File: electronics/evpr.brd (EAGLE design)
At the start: 97.2 x 41.3 mm, 115 parts, among them J1 10118193-0001LF, J2 B4P-VH(LF)(SN), Q1 AOD4184A, Q2 AOD4184A, T3 MMBT2222A, T5 MMBT2222A, U1 BQ2057TTS, U3 ESP32-WROOM-32D, U6 SN74AHCT125DR, U7 TPSM84824MOLR, U8 LTC4353CMSPBFMSOP-16_MS-M, X1 B3P-VH(LF)(SN), X2 B3P-VH(LF)(SN), X3 B3P-VH(LF)(SN)

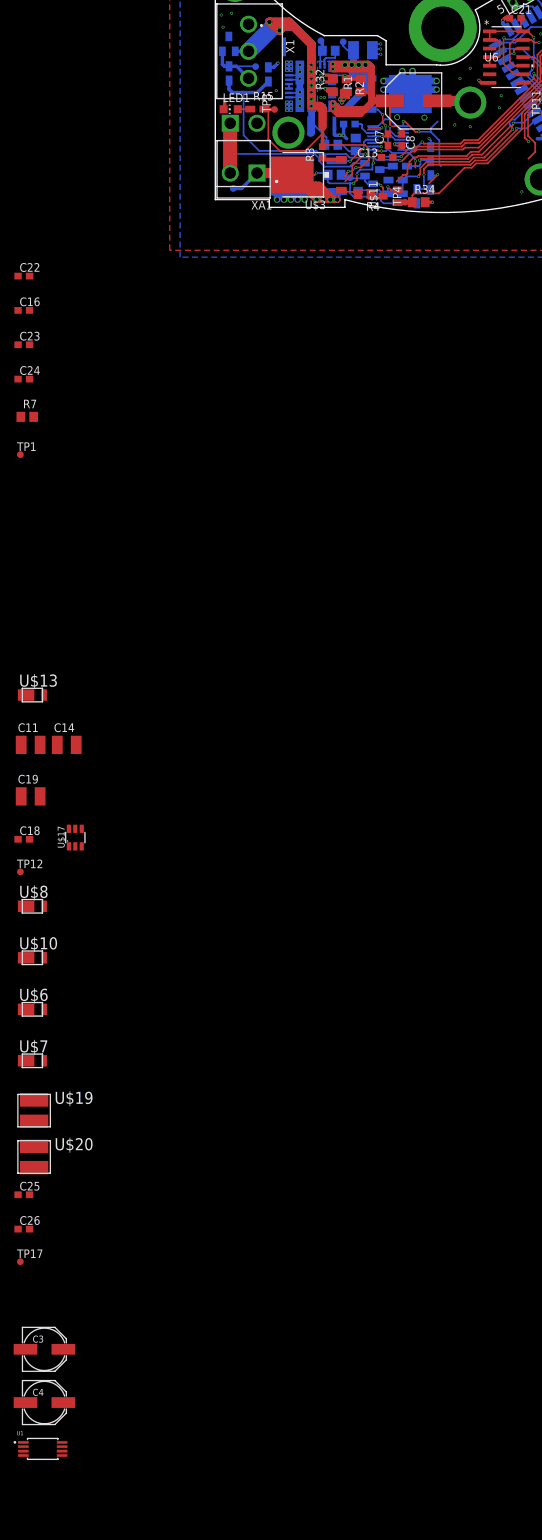
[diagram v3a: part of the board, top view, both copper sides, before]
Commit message: Replaced R31 and R2 with R8 and R32 respectively, 0603 outline and corrected part selection.
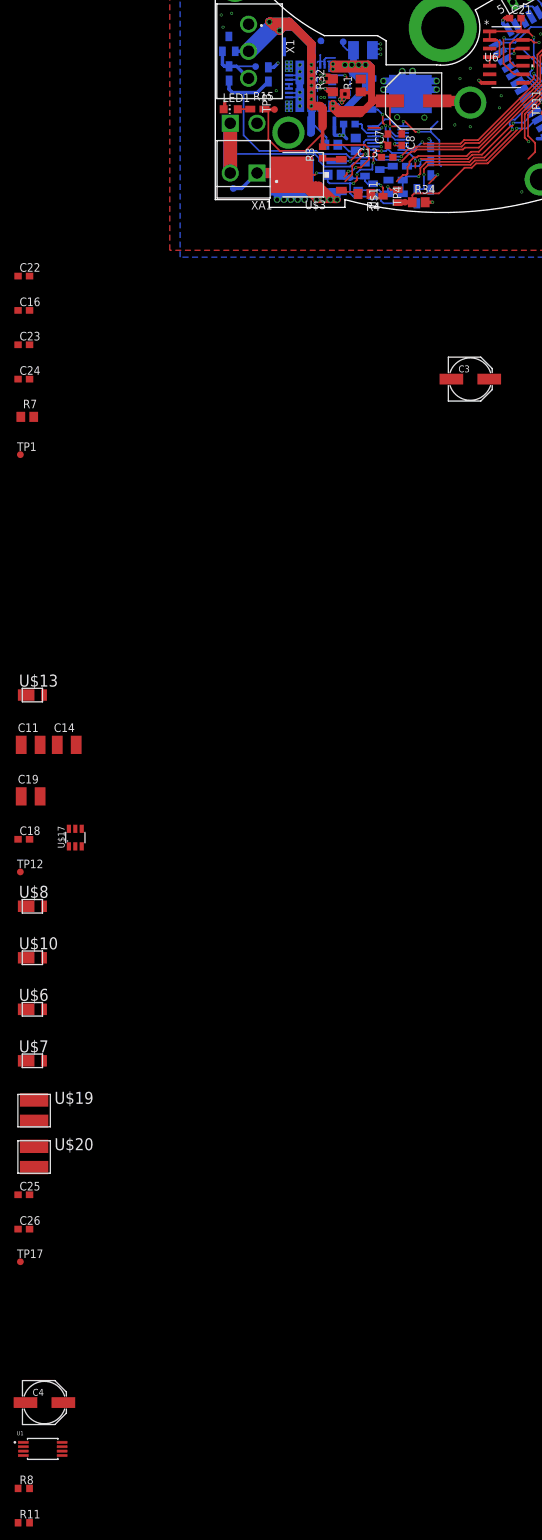
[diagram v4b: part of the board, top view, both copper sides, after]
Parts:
- removed R2: 768Ω 1%, rcl:R0805
- removed R31: 37.4kΩ 1%, rcl:R0805
- added R11: 768Ω 1%, rcl:R0603
- added R8: 37.4kΩ 1%, rcl:R0603
- moved C3 156.7 mm to (4.06, -80.5)
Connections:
- net AGND: now also R11.1, R8.1; no longer R2.2, R31.2
- net N$17: now also R8.2; no longer R31.1
- net N$3: now also R11.2; no longer R2.1
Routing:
- net N$3: track 4.60 -> 2.28 mm
- net AGND: track 12.9 -> 11.0 mm
- net N$17: track 3.54 -> 2.47 mm
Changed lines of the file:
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@@
 <attribute name="VALUE" x="-9.6012" y="-37.719" size="1.27" layer="27" rot="R90"/>
-</element>
-<element name="R2" library="rcl" package="R0805" value="768Ω 1%" x="-14.1986" y="-37.084" smashed="yes" rot="R270">
-<attribute name="COMPONENT" value="RC0402FR-07768RL" x="-14.1986" y="-37.084" size="1.778" layer="27" rot="R270" display="off"/>
-<attribute name="NAME" x="-12.9286" y="-36.449" size="1.27" layer="25" rot="R270"/>
-<attribute name="VALUE" x="-16.7386" y="-36.449" size="1.27" layer="27" rot="R270"/>
-</element>
-<element name="R31" library="rcl" package="R0805" value="37.4kΩ 1%" x="-16.8656" y="-31.9532" smashed="yes" rot="MR0">
-<attribute name="COMPONENT" value="RC0201FR-0737K4L" x="-16.8656" y="-31.9532" size="1.778" layer="28" rot="MR0" display="off"/>
-<attribute name="NAME" x="-16.2306" y="-30.6832" size="1.27" layer="26" rot="MR0"/>
-<attribute name="VALUE" x="-16.2306" y="-34.4932" size="1.27" layer="28" rot="MR0"/>
 </element>
 <element name="C1" library="mccloud" package="CAP_3225" value="10µF" x="-21.59" y="-31.369" smashed="yes" rot="MR180">
@@
 <attribute name="VALUE" x="-62.865" y="-211.582" size="0.0254" layer="27"/>
 </element>
-<element name="C3" library="mccloud" package="OSCON_SVPF_6.3MM" value="56µF" x="-58.928" y="-224.028" smashed="yes">
-<attribute name="COMPONENT" value="APXG250ARA560MF61G" x="-58.928" y="-224.028" size="1.778" layer="27" display="off"/>
-<attribute name="NAME" x="-60.680890625" y="-223.02635" size="1.01768125" layer="25"/>
-<attribute name="VALUE" x="-60.67856875" y="-226.003640625" size="1.01633125" layer="27"/>
+<element name="C3" library="mccloud" package="OSCON_SVPF_6.3MM" value="56µF" x="4.064" y="-80.518" smashed="yes">
+<attribute name="COMPONENT" value="APXG250ARA560MF61G" x="4.064" y="-80.518" size="1.778" layer="27" display="off"/>
+<attribute name="NAME" x="2.311109375" y="-79.51635" size="1.01768125" layer="25"/>
+<attribute name="VALUE" x="2.31343125" y="-82.493640625" size="1.01633125" layer="27"/>
 </element>
 <element name="C4" library="mccloud" package="OSCON_SVPF_6.3MM" value="56µF" x="-58.928" y="-231.902" smashed="yes">
@@
 <attribute name="PACKAGE" value="TSSOP-8 Texas Instruments" x="-59.182" y="-238.76" size="1.778" layer="27" display="off"/>
 <attribute name="VALUE" x="-62.946990625" y="-241.532409375" size="0.610571875" layer="27"/>
+</element>
+<element name="R8" library="rcl" library_urn="urn:adsk.eagle:library:334" package="R0603" package3d_urn="urn:adsk.eagle:package:23555/3" value="37.4kΩ 1%" x="-61.976" y="-244.602" smashed="yes">
+<attribute name="COMPONENT" value="RC0603FR-0737K4L" x="-61.976" y="-244.602" size="1.778" layer="27" display="off"/>
+<attribute name="NAME" x="-62.611" y="-243.967" size="1.27" layer="25"/>
+<attribute name="POPULARITY" value="77" x="-61.976" y="-244.602" size="1.778" layer="27" display="off"/>
+<attribute name="SPICEPREFIX" value="R" x="-61.976" y="-244.602" size="1.778" layer="27" display="off"/>
+<attribute name="VALUE" x="-62.611" y="-246.507" size="1.27" layer="27"/>
+</element>
+<element name="R11" library="rcl" library_urn="urn:adsk.eagle:library:334" package="R0603" package3d_urn="urn:adsk.eagle:package:23555/3" value="768Ω 1%" x="-61.976" y="-249.682" smashed="yes">
+<attribute name="COMPONENT" value="RMCF0603FT768R" x="-61.976" y="-249.682" size="1.778" layer="27" display="off"/>
+<attribute name="NAME" x="-62.611" y="-249.047" size="1.27" layer="25"/>
+<attribute name="POPULARITY" value="77" x="-61.976" y="-249.682" size="1.778" layer="27" display="off"/>
+<attribute name="SPICEPREFIX" value="R" x="-61.976" y="-249.682" size="1.778" layer="27" display="off"/>
+<attribute name="VALUE" x="-62.611" y="-251.587" size="1.27" layer="27"/>
 </element>
 </elements>
@@
 <wire x1="-62.826" y1="-201.168" x2="-53.406" y2="-147.036" width="0" layer="19" extent="1-1"/>
 <wire x1="-62.826" y1="-206.248" x2="-62.826" y2="-201.168" width="0" layer="19" extent="1-1"/>
-<wire x1="-61.728" y1="-224.028" x2="-62.826" y2="-206.248" width="0" layer="19" extent="1-1"/>
-<wire x1="-61.728" y1="-231.902" x2="-61.728" y2="-224.028" width="0" layer="19" extent="1-1"/>
+<wire x1="1.264" y1="-80.518" x2="-62.826" y2="-206.248" width="0" layer="19" extent="1-1"/>
+<wire x1="-61.728" y1="-231.902" x2="1.264" y2="-80.518" width="0" layer="19" extent="1-1"/>
 <wire x1="-56.312" y1="-239.085" x2="-61.728" y2="-231.902" width="0" layer="19" extent="1-1"/>
 </signal>
@@
 <wire x1="-9.0796" y1="-47.7012" x2="-12.762" y2="-49.317" width="0" layer="19" extent="1-1"/>
 <wire x1="-8.0375" y1="-51.0794" x2="-9.0796" y2="-47.7012" width="0" layer="19" extent="1-16"/>
-<wire x1="-56.128" y1="-224.028" x2="-14.5689625" y2="-50.617" width="0" layer="19" extent="1-1"/>
-<wire x1="-56.128" y1="-231.902" x2="-56.128" y2="-224.028" width="0" layer="19" extent="1-1"/>
+<wire x1="6.864" y1="-80.518" x2="-14.5689625" y2="-50.617" width="0" layer="19" extent="1-1"/>
+<wire x1="-56.128" y1="-231.902" x2="6.864" y2="-80.518" width="0" layer="19" extent="1-1"/>
 <wire x1="-56.312" y1="-237.785" x2="-56.128" y2="-231.902" width="0" layer="19" extent="1-1"/>
 <wire x1="-62.052" y1="-239.085" x2="-56.312" y2="-237.785" width="0" layer="19" extent="1-1"/>
@@
 <signal name="N$3">
 <contactref element="R1" pad="2"/>
-<contactref element="R2" pad="1"/>
 <contactref element="U7" pad="2"/>
 <wire x1="-16.358" y1="-35.586" x2="-16.3574" y2="-35.5854" width="0.254" layer="16"/>
@@
 <via x="-14.478" y="-35.5854" extent="1-16" drill="0.254"/>
 <wire x1="-14.478" y1="-35.5854" x2="-14.1986" y2="-35.8648" width="0.254" layer="1"/>
-<wire x1="-14.1986" y1="-35.8648" x2="-14.1986" y2="-36.134" width="0.254" layer="1"/>
-<wire x1="-14.1986" y1="-36.134" x2="-12.1412" y2="-36.134" width="0.508" layer="1"/>
+<contactref element="R11" pad="2"/>
+<wire x1="-16.358" y1="-35.586" x2="-61.126" y2="-249.682" width="0" layer="19" extent="1-16"/>
+<wire x1="-12.1412" y1="-36.134" x2="-14.1986" y2="-35.8648" width="0" layer="19" extent="1-1"/>
 </signal>
 <signal name="N$17">
 <contactref element="U7" pad="24"/>
-<contactref element="R31" pad="1"/>
-<wire x1="-15.9156" y1="-31.9532" x2="-15.9156" y2="-33.02" width="0.254" layer="16"/>
 <wire x1="-15.9156" y1="-33.02" x2="-17.272" y2="-33.02" width="0.254" layer="16"/>
 <wire x1="-17.272" y1="-33.02" x2="-17.526" y2="-33.274" width="0.254" layer="16"/>
 <wire x1="-17.526" y1="-33.274" x2="-17.526" y2="-33.968" width="0.254" layer="16"/>
 <wire x1="-17.526" y1="-33.968" x2="-17.483" y2="-34.011" width="0.254" layer="16"/>
+<contactref element="R8" pad="2"/>
+<wire x1="-17.483" y1="-34.011" x2="-61.126" y2="-244.602" width="0" layer="19" extent="1-16"/>
 </signal>
 <signal name="N$31">
@@
 </signal>
 <signal name="AGND">
-<contactref element="R2" pad="2"/>
-<contactref element="R31" pad="2"/>
 <contactref element="U7" pad="23"/>
 <contactref element="U7" pad="9"/>
 <contactref element="U7" pad="3"/>
 <contactref element="R32" pad="2"/>
-<wire x1="-17.8156" y1="-31.9532" x2="-18.0884375" y2="-32.5664375" width="0.254" layer="16"/>
 <wire x1="-18.0884375" y1="-32.5664375" x2="-18.133" y2="-32.611" width="0.254" layer="16"/>
 <wire x1="-18.133" y1="-32.611" x2="-18.133" y2="-34.011" width="0.254" layer="16"/>
@@
 <contactref element="TP7" pad="TP"/>
 <wire x1="-18.034" y1="-30.48" x2="-17.8156" y2="-30.6984" width="0.508" layer="16"/>
-<wire x1="-17.8156" y1="-30.6984" x2="-17.8156" y2="-31.9532" width="0.508" layer="16"/>
 <wire x1="-15.24" y1="-39.116" x2="-14.9352" y2="-39.624" width="0.508" layer="1"/>
 <wire x1="-14.9352" y1="-39.624" x2="-14.605" y2="-39.116" width="0.508" layer="1"/>
-<wire x1="-14.605" y1="-39.116" x2="-14.1986" y2="-38.034" width="0" layer="19" extent="1-1"/>
+<contactref element="R8" pad="1"/>
+<contactref element="R11" pad="1"/>
+<wire x1="-17.526" y1="-38.862" x2="-18.034" y2="-38.862" width="0" layer="19" extent="1-1"/>
+<wire x1="-18.161" y1="-37.592" x2="-18.034" y2="-38.862" width="0" layer="19" extent="1-1"/>
+<wire x1="-18.034" y1="-36.576" x2="-18.161" y2="-37.592" width="0" layer="19" extent="1-1"/>
+<wire x1="-17.526" y1="-36.576" x2="-18.034" y2="-36.576" width="0" layer="19" extent="1-1"/>
+<wire x1="-16.358" y1="-36.236" x2="-16.764" y2="-36.576" width="0" layer="19" extent="1-16"/>
+<wire x1="-16.256" y1="-36.134" x2="-16.358" y2="-36.236" width="0" layer="19" extent="1-16"/>
+<wire x1="-16.764" y1="-35.56" x2="-16.256" y2="-36.134" width="0" layer="19" extent="1-1"/>
+<wire x1="-18.034" y1="-35.56" x2="-17.526" y2="-35.56" width="0" layer="19" extent="1-1"/>
+<wire x1="-17.483" y1="-40.411" x2="-17.526" y2="-38.862" width="0" layer="19" extent="16-16"/>
+<wire x1="-18.133" y1="-34.011" x2="-18.034" y2="-35.56" width="0" layer="19" extent="16-16"/>
+<wire x1="-17.8156" y1="-30.6984" x2="-18.0884375" y2="-32.5664375" width="0" layer="19" extent="16-16"/>
+<wire x1="-15.24" y1="-39.116" x2="-17.526" y2="-38.862" width="0" layer="19" extent="1-1"/>
+<wire x1="-62.826" y1="-244.602" x2="-17.483" y2="-40.411" width="0" layer="19" extent="1-16"/>
+<wire x1="-62.826" y1="-249.682" x2="-62.826" y2="-244.602" width="0" layer="19" extent="1-1"/>
 </signal>
 <signal name="N$28">

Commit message: Replaced Dot-Star, Servo, PAD connectors with new JST-PA SMD connectors, saving significant board space.
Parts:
- removed J2: B4P-VH(LF)(SN), mccloud:JST_B4P-VH(LF)(SN)
- removed JP1: (no value), pinhead:1X02/90
- added X4: BM03B-PASS-1-TFT(LF)(SN), mccloud:BM03B-PASS-1-TFT(LF)(SN)
- added X5: BM04B-PASS-1-TFT(LF)(SN), mccloud:BM04B-PASS-1-TFT(LF)(SN)
- X2: value B3P-VH(LF)(SN) -> BM02B-PASS-1-TFT(LF)(SN); device B3P-VH_LF__SN_:B3P-VH -> mccloud:BM02B-PASS-1-TFT(LF)(SN)
- X3: value B3P-VH(LF)(SN) -> BM03B-PASS-1-TFT(LF)(SN); device B3P-VH_LF__SN_:B3P-VH -> mccloud:BM03B-PASS-1-TFT(LF)(SN)
- moved X3 267.9 mm to (-68.3, -256.3)
- moved X2 252.8 mm to (-68.3, -245.1), flipped to the top, turned to 0 degrees
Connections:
- net GND: now also X2.P$1, X2.P$5, X2.P$6, X3.P$3, X3.P$5, X3.P$6, X4.P$3, X4.P$5, X4.P$6, X5.P$4, X5.P$5, X5.P$6; no longer J2.4, JP1.1, X2.3, X3.3
- net N$22: now also X5.P$3; no longer J2.3
- net N$27: now also X5.P$2; no longer J2.2
- net N$28: now also X5.P$1; no longer J2.1
- net SERVO1: now also X3.P$2; no longer X2.2
- net SERVO2: now also X4.P$2; no longer X3.2
- net SYS_POWER: now also X2.P$2, X3.P$1, X4.P$1; no longer JP1.2, X2.1, X3.1
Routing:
- net SERVO1: track 36.4 -> 29.7 mm
- net N$22: track 48.6 -> 44.0 mm
- net SERVO2: track 63.8 -> 60.2 mm
- net N$28: track 16.1 -> 13.4 mm
